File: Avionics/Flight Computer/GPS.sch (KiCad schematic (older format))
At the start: 0 parts

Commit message: Restarted initial layout and cleaned up decoupling/RF layout.
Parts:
- added C22: 0.1u, Capacitors_SMD:C_0402, symbol C
- added C23, C53: 0.01u, Capacitors_SMD:C_0402, symbol C
- added J6: 734120110, Connectors_Molex:Molex_Microcoaxial_RF, symbol CONN_COAXIAL
- added R14: 10, Resistors_SMD:R_1210, symbol R
- added U9: MAX-M8W, RF_Modules:U-BLOX-MAX, symbol MAX-M8W
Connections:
- new net: C53.1, R14.1, U9.14 (VCC_RF)
- new net: R14.2, U9.15 (V_ANT)
- new net +3V3: C22.1, C23.1, U9.6 (V_BCKP), U9.7 (VCC_IO), U9.8 (VCC)
- new net GND: C22.2, C23.2, C53.2, J6.2 (Ext), U9.1 (GND), U9.10 (GND), U9.12 (GND)
- new net GPS-EXTINT: U9.5 (EXTINT)
- new net GPS-Pulse: U9.4 (TIMEPULSE)
- new net GPS-Rx: U9.3 (RXD)
- new net GPS-Tx: U9.2 (TXD)
- new net GPS-~Reset: U9.9 (~RESET)
- new net RF_GPS_ANT: J6.1 (In), U9.11 (RF_IN)
- no-connect marks 0 -> 3
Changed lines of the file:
@@
 EESchema Schematic File Version 2
+LIBS:Flight Computer-rescue
 LIBS:device
 LIBS:rfcom
@@
 $Descr A4 11693 8268
 encoding utf-8
-Sheet 5 7
+Sheet 5 9
 Title ""
 Date ""
@@
 Comment4 ""
 $EndDescr
+$Comp
+L CONN_COAXIAL J6
+U 1 1 58AF1B18
+P 6750 3450
+F 0 "J6" H 6850 3426 50  0000 L CNN
+F 1 "734120110" H 6850 3335 50  0000 L CNN
+F 2 "Connectors_Molex:Molex_Microcoaxial_RF" H -350 750 50  0001 C CNN
+F 3 "http://www.molex.com/pdm_docs/sd/734120110_sd.pdf" H -350 750 50  0001 C CNN
+	1    6750 3450
+	1    0    0    -1
+$EndComp
+$Comp
+L GND #PWR056
+U 1 1 58AF392E
+P 6750 3650
+F 0 "#PWR056" H 6800 3700 50  0001 C CNN
+F 1 "GND" H 6755 3477 50  0000 C CNN
+F 2 "" H -50 -100 50  0001 C CNN
+F 3 "" H -50 -100 50  0001 C CNN
+	1    6750 3650
+	1    0    0    -1
+$EndComp
+Wire Wire Line
+	5250 3450 6600 3450
+Text Label 5950 3450 0    60   ~ 0
+RF_GPS_ANT
+$Comp
+L MAX-M8W U9
+U 1 1 58AFAC85
+P 4550 3450
+F 0 "U9" H 4950 4100 50  0000 L CNN
+F 1 "MAX-M8W" H 4000 4100 50  0000 L CNN
+F 2 "RF_Modules:U-BLOX-MAX" H 400 -200 50  0001 C CNN
+F 3 "https://www.u-blox.com/sites/default/files/MAX-M8-FW3_DataSheet_%28UBX-15031506%29.pdf" H -300 -1350 50  0001 C CNN
+	1    4550 3450
+	1    0    0    -1
+$EndComp
+$Comp
+L R R14
+U 1 1 58B486B6
+P 5150 2600
+F 0 "R14" V 5050 2500 50  0000 C CNN
+F 1 "10" V 5150 2600 50  0000 C CNN
+F 2 "Resistors_SMD:R_1210" V -1600 -100 50  0001 C CNN
+F 3 "" V -1320 -100 50  0001 C CNN
+F 4 "1%" V 5050 2700 60  0000 C CNN "Tolerance"
+F 5 "50V" V -1150 -100 60  0001 C CNN "Voltage"
+F 6 "0.5W" V -1050 -100 60  0001 C CNN "Power"
+F 7 "Thin Film" V -950 -100 60  0001 C CNN "Material"
+F 8 "1210" V 5250 2600 60  0000 C CNN "Package"
+	1    5150 2600
+	0    1    1    0
+$EndComp
+Wire Wire Line
+	5000 2600 4750 2600
+Wire Wire Line
+	4750 2600 4750 2650
+Wire Wire Line
+	5300 2600 5900 2600
+Wire Wire Line
+	5600 2600 5600 3150
+Wire Wire Line
+	5600 3150 5250 3150
+$Comp
+L C C53
+U 1 1 58B48916
+P 5900 2850
+F 0 "C53" H 6015 3002 50  0000 L CNN
+F 1 "0.01u" H 6015 2911 50  0000 L CNN
+F 2 "Capacitors_SMD:C_0402" H 188 0   50  0001 C CNN
+F 3 "" H 150 150 50  0001 C CNN
+F 4 "50V" H 6015 2812 60  0000 L CNN "Voltage"
+F 5 "20%" H 6015 2759 60  0001 L CNN "Tolerance"
+F 6 "X7R" H 6015 2706 60  0001 L CNN "Type"
+F 7 "0402" H 6015 2706 60  0000 L CNN "Package"
+	1    5900 2850
+	1    0    0    -1
+$EndComp
+$Comp
+L GND #PWR057
+U 1 1 58B48996
+P 5900 3000
+F 0 "#PWR057" H 5950 3050 50  0001 C CNN
+F 1 "GND" H 5905 2827 50  0000 C CNN
+F 2 "" H -900 -750 50  0001 C CNN
+F 3 "" H -900 -750 50  0001 C CNN
+	1    5900 3000
+	1    0    0    -1
+$EndComp
+Wire Wire Line
+	5900 2600 5900 2700
+Connection ~ 5600 2600
+Wire Wire Line
+	4450 2650 4650 2650
+Connection ~ 4550 2650
+Wire Wire Line
+	4550 2050 4550 2650
+$Comp
+L +3.3V #PWR058
+U 1 1 58B4A068
+P 4550 2050
+F 0 "#PWR058" H 0   -500 50  0001 C CNN
+F 1 "+3.3V" H 4565 2223 50  0000 C CNN
+F 2 "" H 0   -350 50  0001 C CNN
+F 3 "" H 0   -350 50  0001 C CNN
+	1    4550 2050
+	1    0    0    -1
+$EndComp
+$Comp
+L C C23
+U 1 1 58B4A12C
+P 4150 2350
+F 0 "C23" H 4265 2502 50  0000 L CNN
+F 1 "0.01u" H 4265 2411 50  0000 L CNN
+F 2 "Capacitors_SMD:C_0402" H -1562 -500 50  0001 C CNN
+F 3 "" H -1600 -350 50  0001 C CNN
+F 4 "50V" H 4265 2312 60  0000 L CNN "Voltage"
+F 5 "20%" H 4265 2259 60  0001 L CNN "Tolerance"
+F 6 "X7R" H 4265 2206 60  0001 L CNN "Type"
+F 7 "0402" H 4265 2206 60  0000 L CNN "Package"
+	1    4150 2350
+	1    0    0    -1
+$EndComp
+Wire Wire Line
+	3700 2150 4550 2150
+Wire Wire Line
+	4150 2150 4150 2200
+Connection ~ 4550 2150
+$Comp
+L GND #PWR059
+U 1 1 58B4A18F
+P 4150 2500
+F 0 "#PWR059" H 4200 2550 50  0001 C CNN
+F 1 "GND" H 4155 2327 50  0000 C CNN
+F 2 "" H -2650 -1250 50  0001 C CNN
+F 3 "" H -2650 -1250 50  0001 C CNN
+	1    4150 2500
+	1    0    0    -1
+$EndComp
+$Comp
+L C C22
+U 1 1 58B4A1B4
+P 3700 2350
+F 0 "C22" H 3586 2502 50  0000 R CNN
+F 1 "0.1u" H 3586 2411 50  0000 R CNN
+F 2 "Capacitors_SMD:C_0402" H -2012 -500 50  0001 C CNN
+F 3 "" H -2050 -350 50  0001 C CNN
+F 4 "50V" H 3586 2312 60  0000 R CNN "Voltage"
+F 5 "20%" H 3815 2259 60  0001 L CNN "Tolerance"
+F 6 "X7R" H 3815 2206 60  0001 L CNN "Type"
+F 7 "0402" H 3586 2206 60  0000 R CNN "Package"
+	1    3700 2350
+	1    0    0    -1
+$EndComp
+$Comp
+L GND #PWR060
+U 1 1 58B4A1E4
+P 3700 2500
+F 0 "#PWR060" H 3750 2550 50  0001 C CNN
+F 1 "GND" H 3705 2327 50  0000 C CNN
+F 2 "" H -3100 -1250 50  0001 C CNN
+F 3 "" H -3100 -1250 50  0001 C CNN
+	1    3700 2500
+	1    0    0    -1
+$EndComp
+Wire Wire Line
+	3700 2200 3700 2150
+Connection ~ 4150 2150
+NoConn ~ 3850 3250
+NoConn ~ 3850 3150
+NoConn ~ 3850 3750
+$Comp
+L GND #PWR061
+U 1 1 58B4A393
+P 4550 4250
+F 0 "#PWR061" H 4600 4300 50  0001 C CNN
+F 1 "GND" H 4555 4077 50  0000 C CNN
+F 2 "" H -2250 500 50  0001 C CNN
+F 3 "" H -2250 500 50  0001 C CNN
+	1    4550 4250
+	1    0    0    -1
+$EndComp
+Wire Wire Line
+	4450 4250 4650 4250
+Connection ~ 4550 4250
+Wire Wire Line
+	3250 2950 3850 2950
+Wire Wire Line
+	3850 3050 3250 3050
+Text HLabel 3250 3050 0    60   Input ~ 0
+GPS-Rx
+Text HLabel 3250 2950 0    60   Output ~ 0
+GPS-Tx
+Wire Wire Line
+	3850 3450 3250 3450
+Wire Wire Line
+	3850 3550 3250 3550
+Wire Wire Line
+	3250 3650 3850 3650
+Text HLabel 3250 3450 0    60   Input ~ 0
+GPS-EXTINT
+Text HLabel 3250 3550 0    60   Input ~ 0
+GPS-~Reset
+Text HLabel 3250 3650 0    60   Output ~ 0
+GPS-Pulse
 $EndSCHEMATC

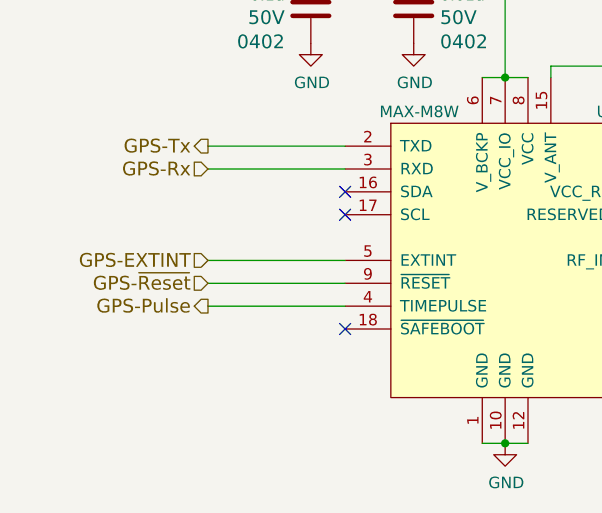
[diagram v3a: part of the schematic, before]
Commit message: Wired up everything and started rearranging layout
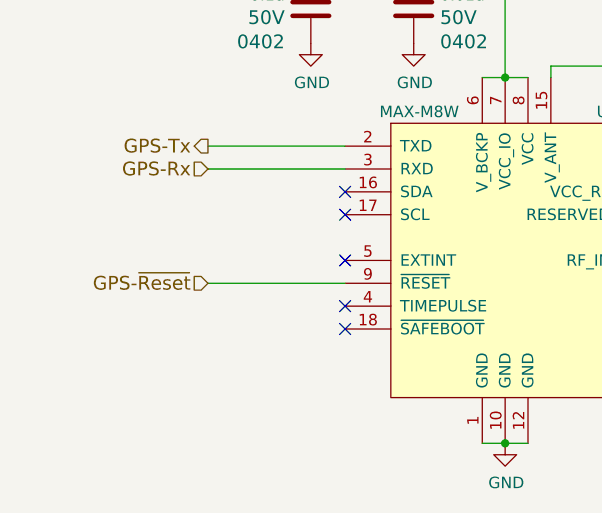
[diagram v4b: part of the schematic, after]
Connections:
- net GPS-EXTINT: no longer names the net of U9.5 (EXTINT)
- net GPS-Pulse: no longer names the net of U9.4 (TIMEPULSE)
- no-connect marks 3 -> 5
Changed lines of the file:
@@
 $Descr A4 11693 8268
 encoding utf-8
-Sheet 5 9
+Sheet 5 8
 Title ""
 Date ""
@@
 GPS-Tx
 Wire Wire Line
-	3850 3450 3250 3450
-Wire Wire Line
 	3850 3550 3250 3550
-Wire Wire Line
-	3250 3650 3850 3650
-Text HLabel 3250 3450 0    60   Input ~ 0
-GPS-EXTINT
 Text HLabel 3250 3550 0    60   Input ~ 0
 GPS-~Reset
-Text HLabel 3250 3650 0    60   Output ~ 0
-GPS-Pulse
+NoConn ~ 3850 3450
+NoConn ~ 3850 3650
 $EndSCHEMATC

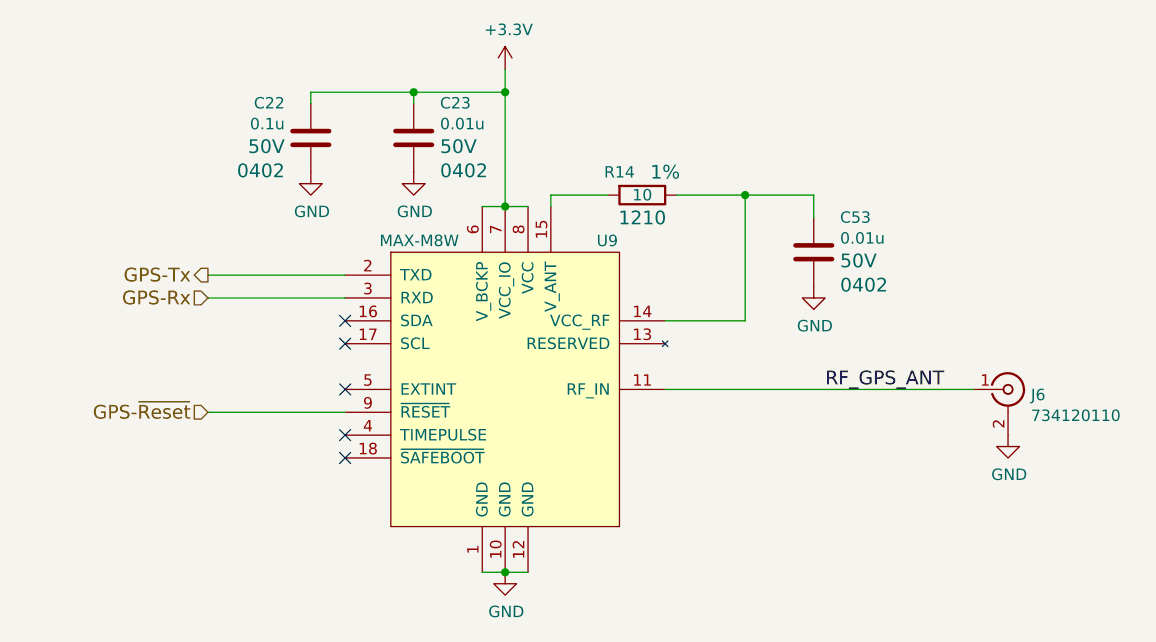
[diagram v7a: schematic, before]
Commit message: Finished routing and DRC check.
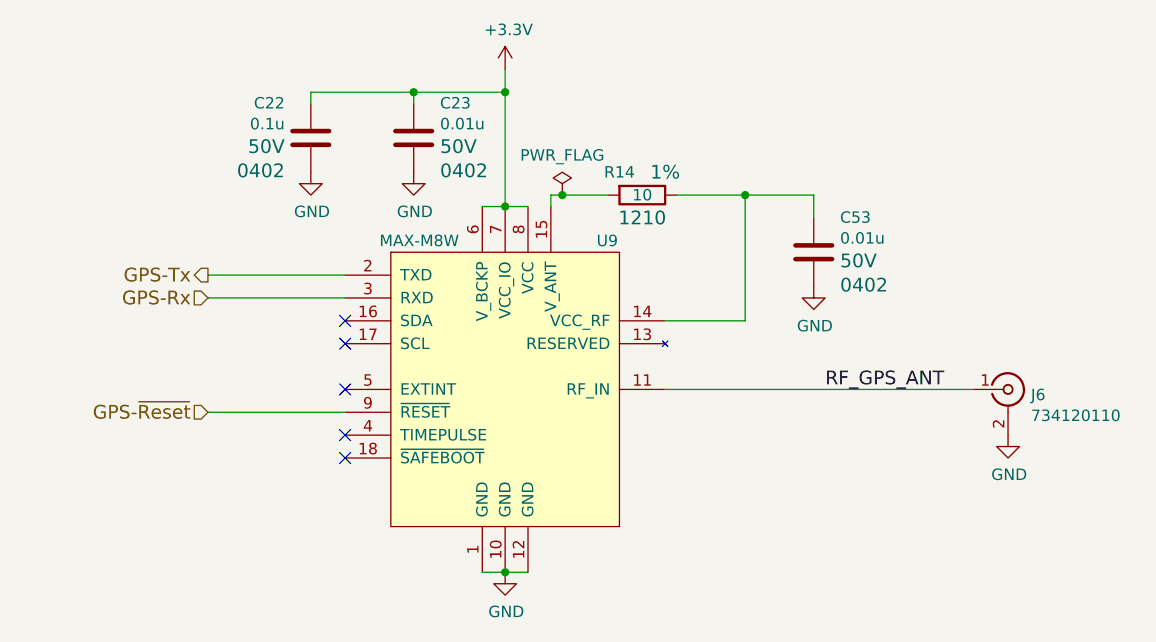
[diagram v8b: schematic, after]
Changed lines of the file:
@@
 $EndComp
 $Comp
-L GND #PWR091
+L GND #PWR0104
 U 1 1 58AF392E
 P 6750 3650
-F 0 "#PWR091" H 6800 3700 50  0001 C CNN
+F 0 "#PWR0104" H 6800 3700 50  0001 C CNN
 F 1 "GND" H 6755 3477 50  0000 C CNN
 F 2 "" H -50 -100 50  0001 C CNN
@@
 $EndComp
 $Comp
-L GND #PWR092
+L GND #PWR0105
 U 1 1 58B48996
 P 5900 3000
-F 0 "#PWR092" H 5950 3050 50  0001 C CNN
+F 0 "#PWR0105" H 5950 3050 50  0001 C CNN
 F 1 "GND" H 5905 2827 50  0000 C CNN
 F 2 "" H -900 -750 50  0001 C CNN
@@
 	4550 2050 4550 2650
 $Comp
-L +3.3V #PWR093
+L +3.3V #PWR0106
 U 1 1 58B4A068
 P 4550 2050
-F 0 "#PWR093" H 0   -500 50  0001 C CNN
+F 0 "#PWR0106" H 0   -500 50  0001 C CNN
 F 1 "+3.3V" H 4565 2223 50  0000 C CNN
 F 2 "" H 0   -350 50  0001 C CNN
@@
 Connection ~ 4550 2150
 $Comp
-L GND #PWR094
+L GND #PWR0107
 U 1 1 58B4A18F
 P 4150 2500
-F 0 "#PWR094" H 4200 2550 50  0001 C CNN
+F 0 "#PWR0107" H 4200 2550 50  0001 C CNN
 F 1 "GND" H 4155 2327 50  0000 C CNN
 F 2 "" H -2650 -1250 50  0001 C CNN
@@
 $EndComp
 $Comp
-L GND #PWR095
+L GND #PWR0108
 U 1 1 58B4A1E4
 P 3700 2500
-F 0 "#PWR095" H 3750 2550 50  0001 C CNN
+F 0 "#PWR0108" H 3750 2550 50  0001 C CNN
 F 1 "GND" H 3705 2327 50  0000 C CNN
 F 2 "" H -3100 -1250 50  0001 C CNN
@@
 NoConn ~ 3850 3750
 $Comp
-L GND #PWR096
+L GND #PWR0109
 U 1 1 58B4A393
 P 4550 4250
-F 0 "#PWR096" H 4600 4300 50  0001 C CNN
+F 0 "#PWR0109" H 4600 4300 50  0001 C CNN
 F 1 "GND" H 4555 4077 50  0000 C CNN
 F 2 "" H -2250 500 50  0001 C CNN
@@
 NoConn ~ 3850 3450
 NoConn ~ 3850 3650
+$Comp
+L PWR_FLAG #FLG0110
+U 1 1 58BF1BFF
+P 4800 2600
+F 0 "#FLG0110" H -450 525 50  0001 C CNN
+F 1 "PWR_FLAG" H 4800 2774 50  0000 C CNN
+F 2 "" H -450 450 50  0001 C CNN
+F 3 "" H -450 450 50  0001 C CNN
+	1    4800 2600
+	1    0    0    -1
+$EndComp
+Connection ~ 4800 2600
 $EndSCHEMATC
